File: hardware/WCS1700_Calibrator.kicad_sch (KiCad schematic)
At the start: 77 parts, among them J1 PJ-002B, J2 560020-0330, J3 282834-8, J4 Conn_01x03_Pin, J5 282834-6, Q1 AO3422, Q2 AO3422, Q3 AO3422, Q4 AO3422, Q5 AO3422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

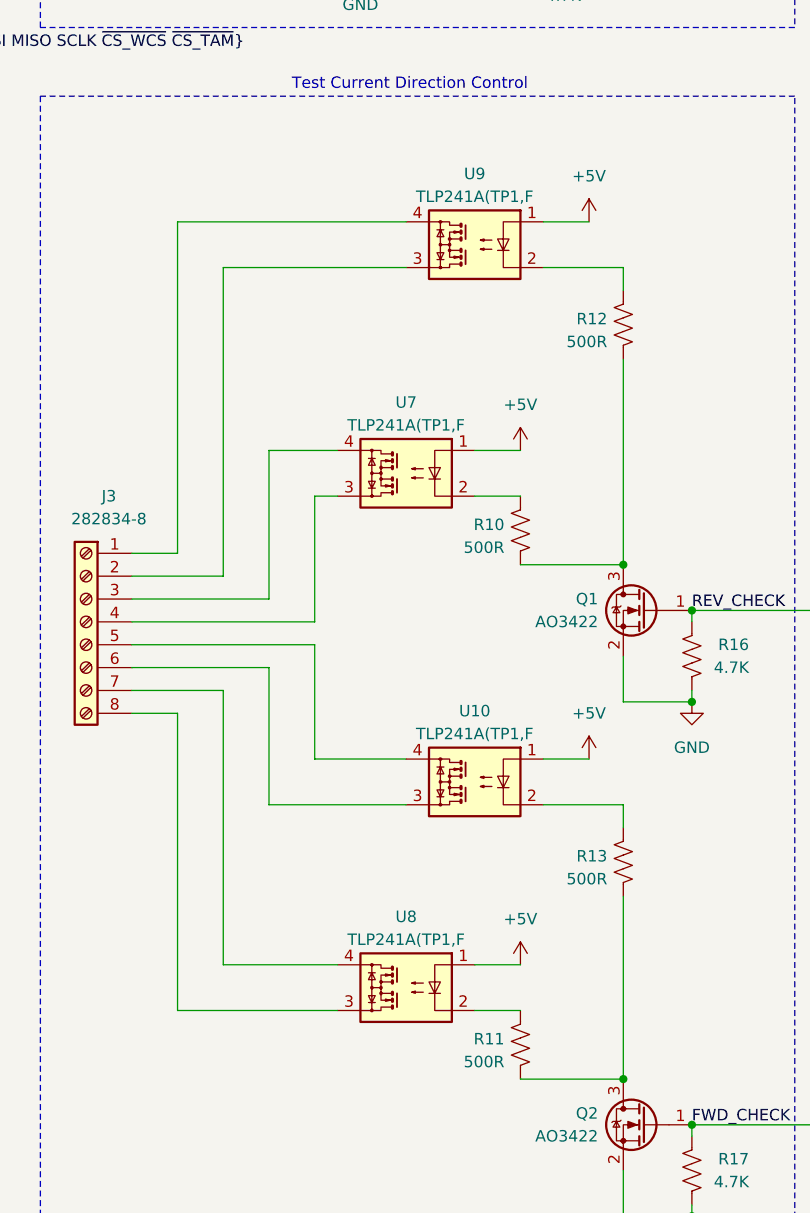
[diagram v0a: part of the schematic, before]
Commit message: Replotted for easier reference designation
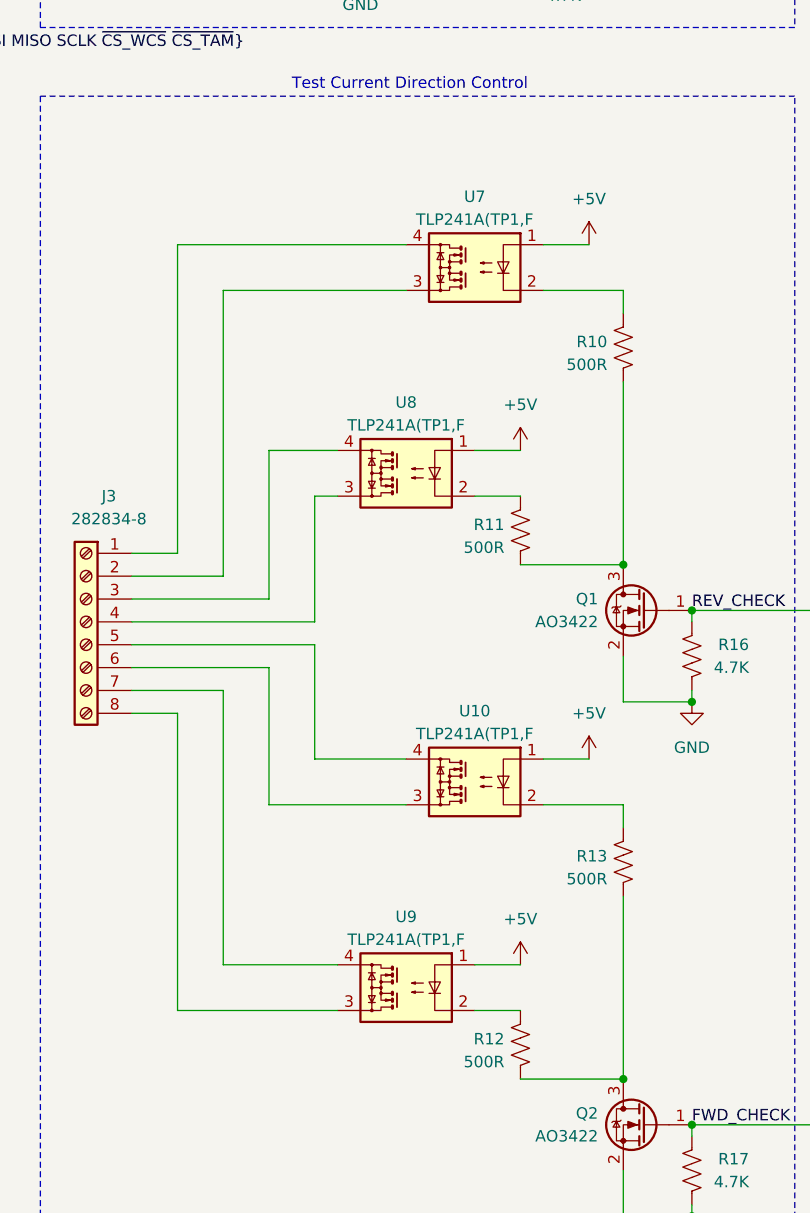
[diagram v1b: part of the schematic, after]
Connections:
- net at Q2.3 (D), R13.2: now also R12.2; no longer R11.2
- net at Q1.3 (D), R10.2: now also R11.2; no longer R12.2
- net at J3.8 (Pin_8): now also U9.3; no longer U8.3
- net at J3.7 (Pin_7): now also U9.4; no longer U8.4
- net at J3.1 (Pin_1): now also U7.4; no longer U9.4
- net at J3.2 (Pin_2): now also U7.3; no longer U9.3
- net at J3.3 (Pin_3): now also U8.4; no longer U7.4
- net at J3.4 (Pin_4): now also U8.3; no longer U7.3

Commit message: Rerouted FETs to match schematic revisions
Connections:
- net at J3.8 (Pin_8): now also U10.3; no longer U9.3
- net at J3.7 (Pin_7): now also U10.4; no longer U9.4
- net at J3.6 (Pin_6): now also U9.3; no longer U10.3
- net at J3.5 (Pin_5): now also U9.4; no longer U10.4
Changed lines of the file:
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@@
     )
   )
+  (symbol (lib_id "Relay_SolidState:TLP222A") (at 195.58 215.9 0) (mirror y) (unit 1)
+    (in_bom yes) (on_board yes) (dnp no)
+    (property "Reference" "U10" (at 195.58 208.026 0)
+      (effects (font (size 1.27 1.27)))
+    )
+    (property "Value" "TLP241A(TP1,F" (at 195.58 210.566 0)
+      (effects (font (size 1.27 1.27)))
+    )
+    (property "Footprint" "OptoDevice:OnSemi_CASE100CY" (at 200.66 220.98 0)
+      (effects (font (size 1.27 1.27) italic) (justify left) hide)
+    )
+    (property "Datasheet" "https://toshiba.semicon-storage.com/info/TLP241A_datasheet_en_20200217.pdf?did=14237&prodName=TLP241A" (at 195.58 215.9 0)
+      (effects (font (size 1.27 1.27)) (justify left) hide)
+    )
+    (pin "1")
+    (pin "2")
+    (pin "3")
+    (pin "4")
+    (instances
+      (project "WCS1700_Calibrator"
+        (path "/1f03928c-0f24-4718-b1ed-d2ed2f2fbec7"
+          (reference "U10") (unit 1)
+        )
+      )
+      (project "Test-Stand-Power-Monitor"
+        (path "/ad7defa1-1037-454f-89aa-6b13c5f4fb2d"
+          (reference "U?") (unit 1)
+        )
+      )
+    )
+  )
   (symbol (lib_id "power:GND") (at 236.22 274.32 0) (mirror y) (unit 1)
     (in_bom yes) (on_board yes) (dnp no) (fields_autoplaced)
@@
     )
   )
-  (symbol (lib_id "Relay_SolidState:TLP222A") (at 195.58 215.9 0) (mirror y) (unit 1)
-    (in_bom yes) (on_board yes) (dnp no)
-    (property "Reference" "U9" (at 195.58 208.026 0)
-      (effects (font (size 1.27 1.27)))
-    )
-    (property "Value" "TLP241A(TP1,F" (at 195.58 210.566 0)
-      (effects (font (size 1.27 1.27)))
-    )
-    (property "Footprint" "OptoDevice:OnSemi_CASE100CY" (at 200.66 220.98 0)
-      (effects (font (size 1.27 1.27) italic) (justify left) hide)
-    )
-    (property "Datasheet" "https://toshiba.semicon-storage.com/info/TLP241A_datasheet_en_20200217.pdf?did=14237&prodName=TLP241A" (at 195.58 215.9 0)
-      (effects (font (size 1.27 1.27)) (justify left) hide)
-    )
-    (pin "1")
-    (pin "2")
-    (pin "3")
-    (pin "4")
-    (instances
-      (project "WCS1700_Calibrator"
-        (path "/1f03928c-0f24-4718-b1ed-d2ed2f2fbec7"
-          (reference "U9") (unit 1)
-        )
-      )
-      (project "Test-Stand-Power-Monitor"
-        (path "/ad7defa1-1037-454f-89aa-6b13c5f4fb2d"
-          (reference "U?") (unit 1)
-        )
-      )
-    )
-  )
   (symbol (lib_id "power:+5V") (at 132.08 179.07 0) (mirror y) (unit 1)
     (in_bom yes) (on_board yes) (dnp no)
@@
     )
   )
-  (symbol (lib_id "Device:R_US") (at 219.71 201.93 0) (mirror y) (unit 1)
-    (in_bom yes) (on_board yes) (dnp no)
-    (property "Reference" "R13" (at 217.932 201.295 0)
-      (effects (font (size 1.27 1.27)) (justify left))
-    )
-    (property "Value" "500R" (at 217.932 203.835 0)
-      (effects (font (size 1.27 1.27)) (justify left))
-    )
-    (property "Footprint" "Resistor_SMD:R_0402_1005Metric_Pad0.72x0.64mm_HandSolder" (at 218.694 202.184 90)
-      (effects (font (size 1.27 1.27)) hide)
-    )
-    (property "Datasheet" "~" (at 219.71 201.93 0)
-      (effects (font (size 1.27 1.27)) hide)
-    )
-    (pin "1")
-    (pin "2")
-    (instances
-      (project "WCS1700_Calibrator"
-        (path "/1f03928c-0f24-4718-b1ed-d2ed2f2fbec7"
-          (reference "R13") (unit 1)
-        )
-      )
-      (project "Test-Stand-Power-Monitor"
-        (path "/ad7defa1-1037-454f-89aa-6b13c5f4fb2d"
-          (reference "R?") (unit 1)
-        )
-      )
-    )
-  )
   (symbol (lib_id "power:GND") (at 288.29 238.76 0) (unit 1)
     (in_bom yes) (on_board yes) (dnp no) (fields_autoplaced)
@@
     )
   )
+  (symbol (lib_id "Relay_SolidState:TLP222A") (at 203.2 193.04 0) (mirror y) (unit 1)
+    (in_bom yes) (on_board yes) (dnp no)
+    (property "Reference" "U9" (at 203.2 185.166 0)
+      (effects (font (size 1.27 1.27)))
+    )
+    (property "Value" "TLP241A(TP1,F" (at 203.2 187.706 0)
+      (effects (font (size 1.27 1.27)))
+    )
+    (property "Footprint" "OptoDevice:OnSemi_CASE100CY" (at 208.28 198.12 0)
+      (effects (font (size 1.27 1.27) italic) (justify left) hide)
+    )
+    (property "Datasheet" "https://toshiba.semicon-storage.com/info/TLP241A_datasheet_en_20200217.pdf?did=14237&prodName=TLP241A" (at 203.2 193.04 0)
+      (effects (font (size 1.27 1.27)) (justify left) hide)
+    )
+    (pin "1")
+    (pin "2")
+    (pin "3")
+    (pin "4")
+    (instances
+      (project "WCS1700_Calibrator"
+        (path "/1f03928c-0f24-4718-b1ed-d2ed2f2fbec7"
+          (reference "U9") (unit 1)
+        )
+      )
+      (project "Test-Stand-Power-Monitor"
+        (path "/ad7defa1-1037-454f-89aa-6b13c5f4fb2d"
+          (reference "U?") (unit 1)
+        )
+      )
+    )
+  )
   (symbol (lib_id "power:+5V") (at 351.79 210.82 0) (unit 1)
     (in_bom yes) (on_board yes) (dnp no) (fields_autoplaced)
@@
     )
   )
-  (symbol (lib_id "Relay_SolidState:TLP222A") (at 203.2 193.04 0) (mirror y) (unit 1)
-    (in_bom yes) (on_board yes) (dnp no)
-    (property "Reference" "U10" (at 203.2 185.166 0)
-      (effects (font (size 1.27 1.27)))
-    )
-    (property "Value" "TLP241A(TP1,F" (at 203.2 187.706 0)
-      (effects (font (size 1.27 1.27)))
-    )
-    (property "Footprint" "OptoDevice:OnSemi_CASE100CY" (at 208.28 198.12 0)
-      (effects (font (size 1.27 1.27) italic) (justify left) hide)
-    )
-    (property "Datasheet" "https://toshiba.semicon-storage.com/info/TLP241A_datasheet_en_20200217.pdf?did=14237&prodName=TLP241A" (at 203.2 193.04 0)
-      (effects (font (size 1.27 1.27)) (justify left) hide)
-    )
-    (pin "1")
-    (pin "2")
-    (pin "3")
-    (pin "4")
-    (instances
-      (project "WCS1700_Calibrator"
-        (path "/1f03928c-0f24-4718-b1ed-d2ed2f2fbec7"
-          (reference "U10") (unit 1)
-        )
-      )
-      (project "Test-Stand-Power-Monitor"
-        (path "/ad7defa1-1037-454f-89aa-6b13c5f4fb2d"
-          (reference "U?") (unit 1)
-        )
-      )
-    )
-  )
   (symbol (lib_name "MCP3208_1") (lib_id "Analog_ADC:MCP3208") (at 106.68 71.12 0) (unit 1)
     (in_bom yes) (on_board yes) (dnp no) (fields_autoplaced)
@@
     )
   )
-  (symbol (lib_id "Device:R_US") (at 208.28 222.25 0) (mirror y) (unit 1)
-    (in_bom yes) (on_board yes) (dnp no)
-    (property "Reference" "R12" (at 206.502 221.615 0)
-      (effects (font (size 1.27 1.27)) (justify left))
-    )
-    (property "Value" "500R" (at 206.502 224.155 0)
-      (effects (font (size 1.27 1.27)) (justify left))
-    )
-    (property "Footprint" "Resistor_SMD:R_0402_1005Metric_Pad0.72x0.64mm_HandSolder" (at 207.264 222.504 90)
-      (effects (font (size 1.27 1.27)) hide)
-    )
-    (property "Datasheet" "~" (at 208.28 222.25 0)
-      (effects (font (size 1.27 1.27)) hide)
-    )
-    (pin "1")
-    (pin "2")
-    (instances
-      (project "WCS1700_Calibrator"
-        (path "/1f03928c-0f24-4718-b1ed-d2ed2f2fbec7"
-          (reference "R12") (unit 1)
-        )
-      )
-      (project "Test-Stand-Power-Monitor"
-        (path "/ad7defa1-1037-454f-89aa-6b13c5f4fb2d"
-          (reference "R?") (unit 1)
-        )
-      )
-    )
-  )
   (symbol (lib_id "power:+5V") (at 351.79 181.61 0) (unit 1)
     (in_bom yes) (on_board yes) (dnp no) (fields_autoplaced)
@@
     )
   )
+  (symbol (lib_id "Device:R_US") (at 219.71 201.93 0) (mirror y) (unit 1)
+    (in_bom yes) (on_board yes) (dnp no)
+    (property "Reference" "R12" (at 217.932 201.295 0)
+      (effects (font (size 1.27 1.27)) (justify left))
+    )
+    (property "Value" "500R" (at 217.932 203.835 0)
+      (effects (font (size 1.27 1.27)) (justify left))
+    )
+    (property "Footprint" "Resistor_SMD:R_0402_1005Metric_Pad0.72x0.64mm_HandSolder" (at 218.694 202.184 90)
+      (effects (font (size 1.27 1.27)) hide)
+    )
+    (property "Datasheet" "~" (at 219.71 201.93 0)
+      (effects (font (size 1.27 1.27)) hide)
+    )
+    (pin "1")
+    (pin "2")
+    (instances
+      (project "WCS1700_Calibrator"
+        (path "/1f03928c-0f24-4718-b1ed-d2ed2f2fbec7"
+          (reference "R12") (unit 1)
+        )
+      )
+      (project "Test-Stand-Power-Monitor"
+        (path "/ad7defa1-1037-454f-89aa-6b13c5f4fb2d"
+          (reference "R?") (unit 1)
+        )
+      )
+    )
+  )
   (symbol (lib_id "power:GND") (at 203.2 45.72 0) (mirror y) (unit 1)
     (in_bom yes) (on_board yes) (dnp no)
@@
         )
       )
+    )
+  )
+  (symbol (lib_id "Device:R_US") (at 208.28 222.25 0) (mirror y) (unit 1)
+    (in_bom yes) (on_board yes) (dnp no)
+    (property "Reference" "R13" (at 206.502 221.615 0)
+      (effects (font (size 1.27 1.27)) (justify left))
+    )
+    (property "Value" "500R" (at 206.502 224.155 0)
+      (effects (font (size 1.27 1.27)) (justify left))
+    )
+    (property "Footprint" "Resistor_SMD:R_0402_1005Metric_Pad0.72x0.64mm_HandSolder" (at 207.264 222.504 90)
+      (effects (font (size 1.27 1.27)) hide)
+    )
+    (property "Datasheet" "~" (at 208.28 222.25 0)
+      (effects (font (size 1.27 1.27)) hide)
+    )
+    (pin "1")
+    (pin "2")
+    (instances
+      (project "WCS1700_Calibrator"
+        (path "/1f03928c-0f24-4718-b1ed-d2ed2f2fbec7"
+          (reference "R13") (unit 1)
+        )
+      )
+      (project "Test-Stand-Power-Monitor"
+        (path "/ad7defa1-1037-454f-89aa-6b13c5f4fb2d"
+          (reference "R?") (unit 1)
+        )
+      )

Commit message: Added output enable 3.3V pull-up resistor on U6
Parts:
- added R26: 4.7K, Resistor_SMD:R_0402_1005Metric_Pad0.72x0.64mm_HandSolder, symbol Device:R_US
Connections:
- net +3V3: now also R26.1; no longer U6.8 (OE)
- new net: R26.2, U6.8 (OE)
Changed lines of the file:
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@@
     (stroke (width 0) (type default))
   )
+  (wire (pts (xy 200.66 60.96) (xy 209.55 60.96))
+    (stroke (width 0) (type default))
+  )
   (wire (pts (xy 180.34 180.34) (xy 180.34 195.58))
     (stroke (width 0) (type default))
@@
     (stroke (width 0) (type default))
   )
-  (wire (pts (xy 203.2 60.96) (xy 200.66 60.96))
-    (stroke (width 0) (type default))
-  )
   (wire (pts (xy 292.1 78.74) (xy 325.12 78.74))
     (stroke (width 0) (type default))
@@
     )
   )
-  (symbol (lib_id "power:+3V3") (at 203.2 60.96 0) (unit 1)
+  (symbol (lib_id "power:+3V3") (at 209.55 53.34 0) (unit 1)
     (in_bom yes) (on_board yes) (dnp no)
-    (property "Reference" "#PWR035" (at 203.2 64.77 0)
+    (property "Reference" "#PWR035" (at 209.55 57.15 0)
       (effects (font (size 1.27 1.27)) hide)
     )
-    (property "Value" "+3V3" (at 203.2 56.896 0)
+    (property "Value" "+3V3" (at 209.55 49.276 0)
       (effects (font (size 1.27 1.27)))
     )
-    (property "Footprint" "" (at 203.2 60.96 0)
+    (property "Footprint" "" (at 209.55 53.34 0)
       (effects (font (size 1.27 1.27)) hide)
     )
-    (property "Datasheet" "" (at 203.2 60.96 0)
+    (property "Datasheet" "" (at 209.55 53.34 0)
       (effects (font (size 1.27 1.27)) hide)
     )
@@
         )
       )
+    )
+  )
+  (symbol (lib_id "Device:R_US") (at 209.55 57.15 0) (mirror y) (unit 1)
+    (in_bom yes) (on_board yes) (dnp no)
+    (property "Reference" "R26" (at 215.9 55.88 0)
+      (effects (font (size 1.27 1.27)) (justify left))
+    )
+    (property "Value" "4.7K" (at 215.9 58.42 0)
+      (effects (font (size 1.27 1.27)) (justify left))
+    )
+    (property "Footprint" "Resistor_SMD:R_0402_1005Metric_Pad0.72x0.64mm_HandSolder" (at 208.534 57.404 90)
+      (effects (font (size 1.27 1.27)) hide)
+    )
+    (property "Datasheet" "~" (at 209.55 57.15 0)
+      (effects (font (size 1.27 1.27)) hide)
+    )
+    (pin "1")
+    (pin "2")
+    (instances
+      (project "WCS1700_Calibrator"
+        (path "/1f03928c-0f24-4718-b1ed-d2ed2f2fbec7"
+          (reference "R26") (unit 1)
+        )
+      )
